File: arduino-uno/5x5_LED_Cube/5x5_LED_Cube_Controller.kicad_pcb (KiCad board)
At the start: 2 copper layers, 11 parts, among them Q1 DMG2305UX, Q2 DMG2305UX, Q3 DMG2305UX, Q4 DMG2305UX, Q5 DMG2305UX, U1 TLC5940NT, U2 TLC5940NT

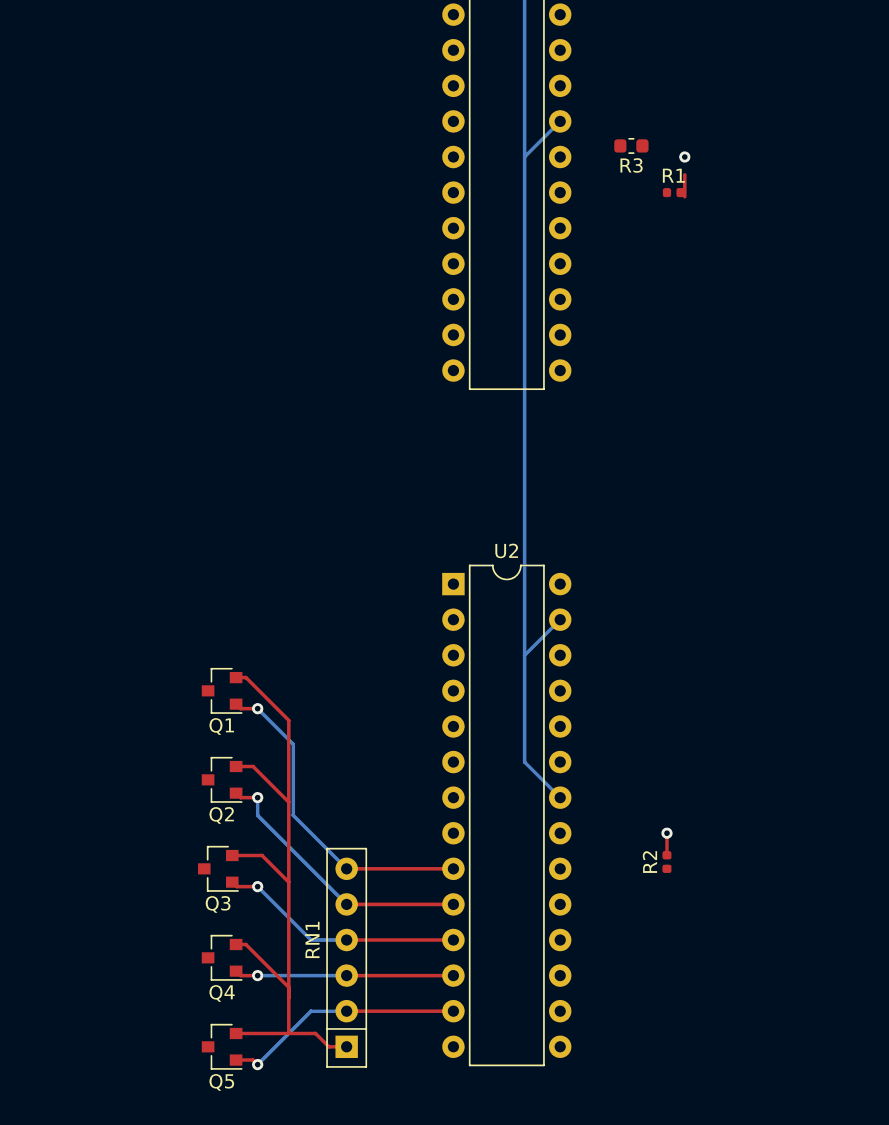
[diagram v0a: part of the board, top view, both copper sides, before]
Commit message: Added headers for layers and arduino input
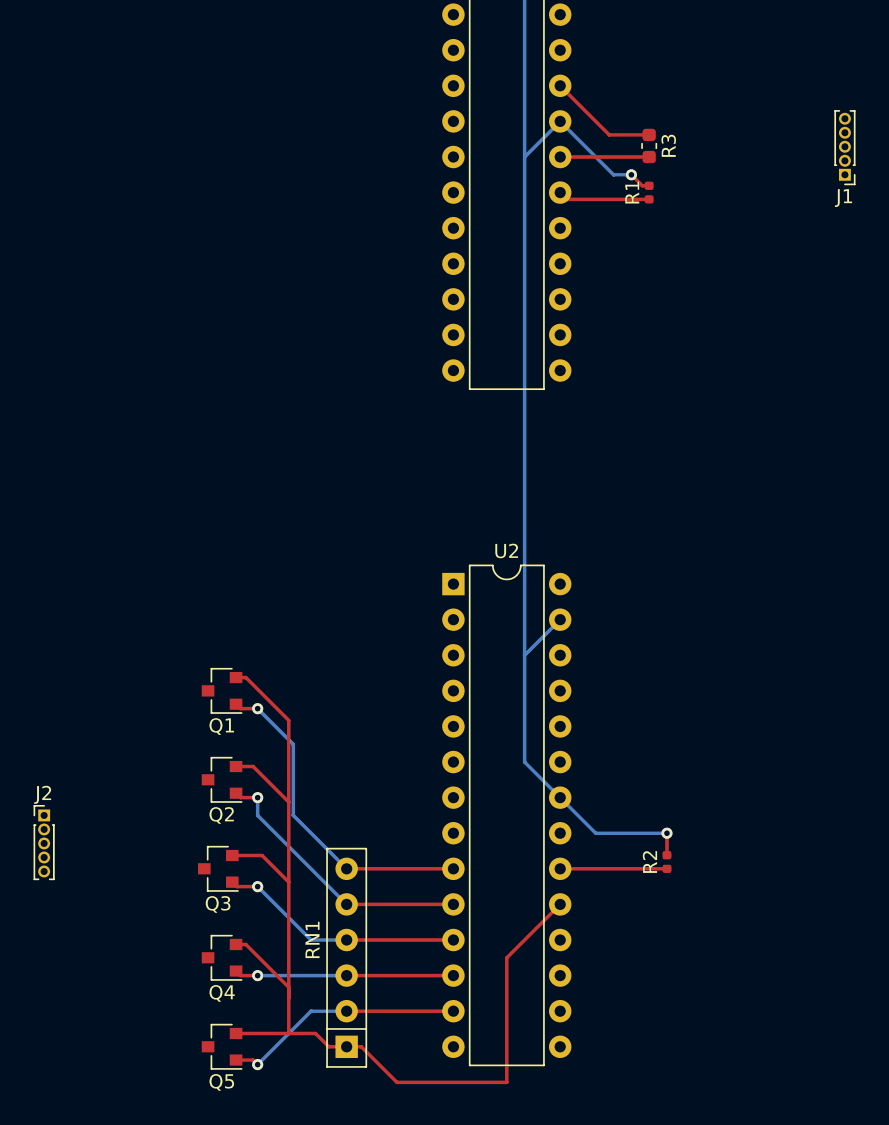
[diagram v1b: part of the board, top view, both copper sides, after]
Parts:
- added J1: Conn_01x05, Connector_PinHeader_1.00mm:PinHeader_1x05_P1.00mm_Vertical, F.Cu at (246.4, 61.0)
- added J2: Conn_01x05, Connector_PinHeader_1.00mm:PinHeader_1x05_P1.00mm_Vertical, F.Cu at (189.2, 106.7)
- moved R1 1.75 mm to (232.4, 62.2), turned to 90 degrees
- moved R3 1.27 mm to (232.4, 58.9), turned to 270 degrees
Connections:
- Q1 pad 3: /5x5_LED_Cube_Matrix/Layer1 -> /Layer1
- Q2 pad 3: /5x5_LED_Cube_Matrix/Layer2 -> /Layer2
- Q3 pad 3: /5x5_LED_Cube_Matrix/Layer3 -> /Layer3
- Q4 pad 3: /5x5_LED_Cube_Matrix/Layer4 -> /Layer4
- Q5 pad 3: /5x5_LED_Cube_Matrix/Layer5 -> /Layer5
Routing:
- net +5V: track 51.1 -> 84.2 mm
- net GND: track 73.4 -> 88.7 mm
- net /ArduinoD10: track 0.00 -> 7.80 mm
- net Net-(R2-Pad1): track 0.00 -> 7.62 mm
- net Net-(R1-Pad1): track 0.00 -> 6.55 mm

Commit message: Updated PCB to latest schematic changes
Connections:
- net /5x5_LED_Cube_Matrix/LED1 renamed /LED1
- net /5x5_LED_Cube_Matrix/LED10 renamed /LED10
- net /5x5_LED_Cube_Matrix/LED11 renamed /LED11
- net /5x5_LED_Cube_Matrix/LED12 renamed /LED12
- net /5x5_LED_Cube_Matrix/LED13 renamed /LED13
- net /5x5_LED_Cube_Matrix/LED14 renamed /LED14
- net /5x5_LED_Cube_Matrix/LED15 renamed /LED15
- net /5x5_LED_Cube_Matrix/LED16 renamed /LED16
- net /5x5_LED_Cube_Matrix/LED17 renamed /LED17
- net /5x5_LED_Cube_Matrix/LED18 renamed /LED18
- net /5x5_LED_Cube_Matrix/LED19 renamed /LED19
- net /5x5_LED_Cube_Matrix/LED2 renamed /LED2
- net /5x5_LED_Cube_Matrix/LED20 renamed /LED20
- net /5x5_LED_Cube_Matrix/LED21 renamed /LED21
- net /5x5_LED_Cube_Matrix/LED22 renamed /LED22
- net /5x5_LED_Cube_Matrix/LED23 renamed /LED23
- net /5x5_LED_Cube_Matrix/LED24 renamed /LED24
- net /5x5_LED_Cube_Matrix/LED25 renamed /LED25
- net /5x5_LED_Cube_Matrix/LED3 renamed /LED3
- net /5x5_LED_Cube_Matrix/LED4 renamed /LED4
- net /5x5_LED_Cube_Matrix/LED5 renamed /LED5
- net /5x5_LED_Cube_Matrix/LED6 renamed /LED6
- net /5x5_LED_Cube_Matrix/LED7 renamed /LED7
- net /5x5_LED_Cube_Matrix/LED8 renamed /LED8
- net /5x5_LED_Cube_Matrix/LED9 renamed /LED9
- net Net-(Q1-Pad1) renamed /Layer1Gate
- net Net-(Q2-Pad1) renamed /Layer2Gate
- net Net-(Q3-Pad1) renamed /Layer3Gate
- net Net-(Q4-Pad1) renamed /Layer4Gate
- net Net-(Q5-Pad1) renamed /Layer5Gate
- net Net-(R1-Pad1) renamed /IREF1
- net Net-(R2-Pad1) renamed /IREF2

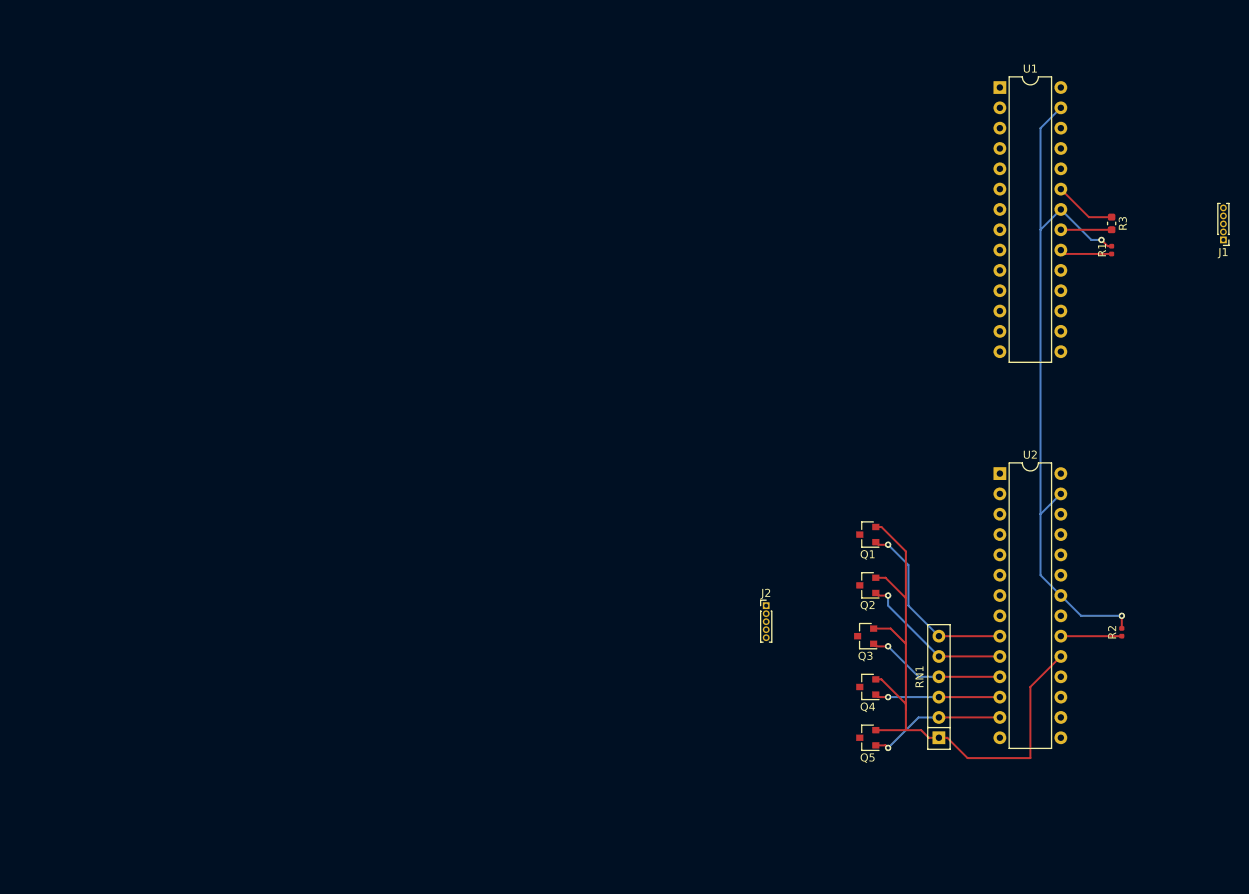
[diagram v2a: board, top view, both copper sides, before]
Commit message: Routed more PCB traces and added power header
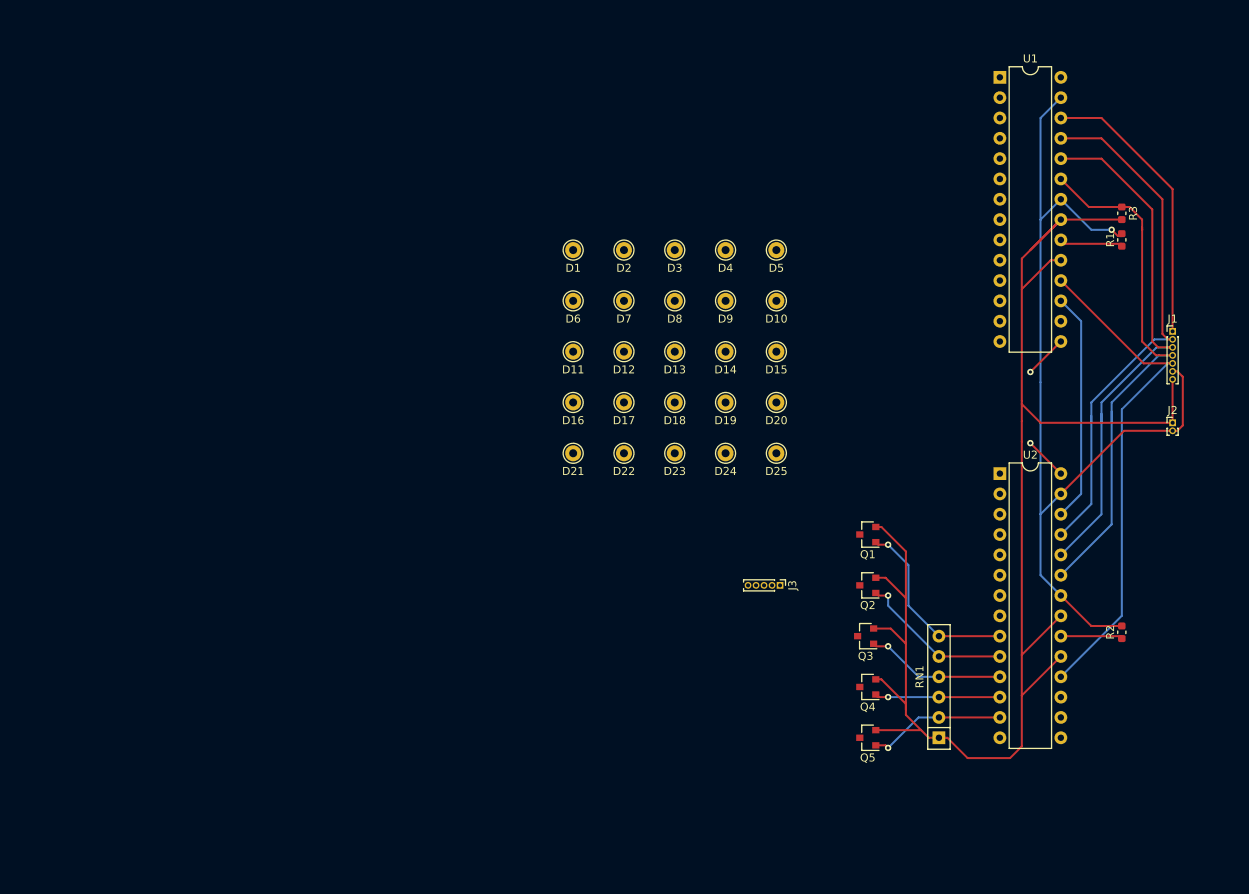
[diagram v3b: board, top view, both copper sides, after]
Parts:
- added D1: LED, Connector_Pin:Pin_D1.0mm_L10.0mm, F.Cu at (165.1, 62.2)
- added D10: LED, Connector_Pin:Pin_D1.0mm_L10.0mm, F.Cu at (190.5, 68.6)
- added D11: LED, Connector_Pin:Pin_D1.0mm_L10.0mm, F.Cu at (165.1, 74.9)
- added D12: LED, Connector_Pin:Pin_D1.0mm_L10.0mm, F.Cu at (171.4, 74.9)
- added D13: LED, Connector_Pin:Pin_D1.0mm_L10.0mm, F.Cu at (177.8, 74.9)
- added D14: LED, Connector_Pin:Pin_D1.0mm_L10.0mm, F.Cu at (184.2, 74.9)
- added D15: LED, Connector_Pin:Pin_D1.0mm_L10.0mm, F.Cu at (190.5, 74.9)
- added D16: LED, Connector_Pin:Pin_D1.0mm_L10.0mm, F.Cu at (165.1, 81.3)
- added D17: LED, Connector_Pin:Pin_D1.0mm_L10.0mm, F.Cu at (171.4, 81.3)
- added D18: LED, Connector_Pin:Pin_D1.0mm_L10.0mm, F.Cu at (177.8, 81.3)
- added D19: LED, Connector_Pin:Pin_D1.0mm_L10.0mm, F.Cu at (184.2, 81.3)
- added D2: LED, Connector_Pin:Pin_D1.0mm_L10.0mm, F.Cu at (171.4, 62.2)
- added D20: LED, Connector_Pin:Pin_D1.0mm_L10.0mm, F.Cu at (190.5, 81.3)
- added D21: LED, Connector_Pin:Pin_D1.0mm_L10.0mm, F.Cu at (165.1, 87.6)
- added D22: LED, Connector_Pin:Pin_D1.0mm_L10.0mm, F.Cu at (171.4, 87.6)
- added D23: LED, Connector_Pin:Pin_D1.0mm_L10.0mm, F.Cu at (177.8, 87.6)
- added D24: LED, Connector_Pin:Pin_D1.0mm_L10.0mm, F.Cu at (184.2, 87.6)
- added D25: LED, Connector_Pin:Pin_D1.0mm_L10.0mm, F.Cu at (190.5, 87.6)
- added D3: LED, Connector_Pin:Pin_D1.0mm_L10.0mm, F.Cu at (177.8, 62.2)
- added D4: LED, Connector_Pin:Pin_D1.0mm_L10.0mm, F.Cu at (184.2, 62.2)
- added D5: LED, Connector_Pin:Pin_D1.0mm_L10.0mm, F.Cu at (190.5, 62.2)
- added D6: LED, Connector_Pin:Pin_D1.0mm_L10.0mm, F.Cu at (165.1, 68.6)
- added D7: LED, Connector_Pin:Pin_D1.0mm_L10.0mm, F.Cu at (171.4, 68.6)
- added D8: LED, Connector_Pin:Pin_D1.0mm_L10.0mm, F.Cu at (177.8, 68.6)
- added D9: LED, Connector_Pin:Pin_D1.0mm_L10.0mm, F.Cu at (184.2, 68.6)
- added J2: Power, Connector_PinHeader_1.00mm:PinHeader_1x02_P1.00mm_Vertical, F.Cu at (240.0, 83.8)
- J1: value Conn_01x05 -> Arduino; footprint Connector_PinHeader_1.00mm:PinHeader_1x05_P1.00mm_Vertical -> Connector_PinHeader_1.00mm:PinHeader_1x07_P1.00mm_Vertical
- J3: renamed from J2; value Conn_01x05 -> Layers
- R1, R2: footprint Resistor_SMD:R_0402_1005Metric -> Resistor_SMD:R_0603_1608Metric
- moved J1 13.1 mm to (240.0, 72.4), turned to 0 degrees
- moved J3 3.07 mm to (191.0, 104.1), turned to 270 degrees
- moved R3 1.80 mm to (233.7, 57.6)
- moved R1 1.80 mm to (233.7, 61.0)
- moved U1 1.27 mm to (218.4, 40.6)
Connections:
- J1 pad 1: /ArduinoD3 -> /ArduinoD11(SIN)
- J1 pad 2: /ArduinoD9 -> /ArduinoD13(SCLK)
- J1 pad 3: /ArduinoD10 -> /ArduinoD9(XLAT)
- J1 pad 4: /ArduinoD11 -> /ArduinoD10(BLANK)
- J1 pad 5: /ArduinoD13 -> /ArduinoD3(GSCLK)
- R3 pad 1: /ArduinoD10 -> /ArduinoD10(BLANK)
- U1 pad 17: Net-(U1-Pad17) -> /SOUT1
- U1 pad 18: /ArduinoD3 -> /ArduinoD3(GSCLK)
- U1 pad 23: /ArduinoD10 -> /ArduinoD10(BLANK)
- U1 pad 24: /ArduinoD9 -> /ArduinoD9(XLAT)
- U1 pad 25: /ArduinoD13 -> /ArduinoD13(SCLK)
- U1 pad 26: Net-(U1-Pad26) -> /ArduinoD11(SIN)
- U2 pad 17: Net-(U1-Pad26) -> Net-(U2-Pad17)
- U2 pad 18: /ArduinoD3 -> /ArduinoD3(GSCLK)
- U2 pad 23: /ArduinoD10 -> /ArduinoD10(BLANK)
- U2 pad 24: /ArduinoD9 -> /ArduinoD9(XLAT)
- U2 pad 25: /ArduinoD13 -> /ArduinoD13(SCLK)
- U2 pad 26: /ArduinoD11 -> /SOUT1
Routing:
- net +5V: track 84.2 -> 192.0 mm
- net /ArduinoD9(XLAT): track 0.00 -> 68.1 mm
- net /ArduinoD10(BLANK): track 0.00 -> 68.0 mm
- net /ArduinoD13(SCLK): track 0.00 -> 66.6 mm
- net /ArduinoD3(GSCLK): track 0.00 -> 63.6 mm
- net /ArduinoD11(SIN): track 0.00 -> 35.4 mm
- net /SOUT1: track 0.00 -> 28.8 mm
- net GND: track 88.7 -> 116.7 mm, vias 2 -> 1
- net /ArduinoD10: track 7.80 -> 0.00 mm
- net /LED17: track 0.00 -> 5.39 mm, vias 0 -> 1
- net /LED16: track 0.00 -> 5.39 mm, vias 0 -> 1
- net /IREF1: track 6.55 -> 7.82 mm

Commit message: Finished PCB routing
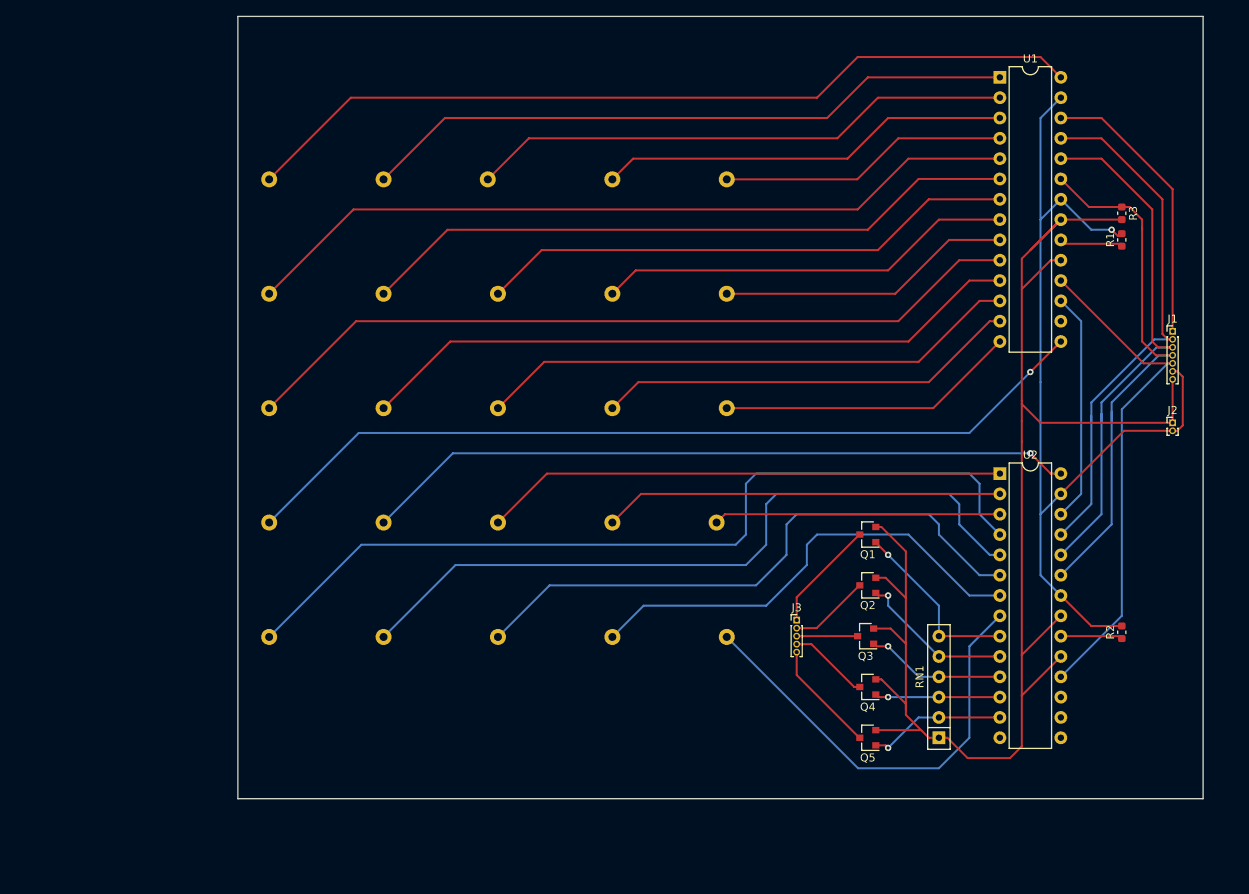
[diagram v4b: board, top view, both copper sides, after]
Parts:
- D1, D10, D11, D12, D13, D14, D15, D16, D17, D18, D19, D2, D20, D21, D22, D23, D24, D25, D3, D4, D5, D6, D7, D8, D9: moved to B.Cu
- moved D21 44.4 mm to (127.1, 110.6)
- moved D16 40.9 mm to (127.1, 96.3)
- moved D1 39.0 mm to (127.1, 53.4)
- moved D11 38.7 mm to (127.1, 82.0)
- moved D6 38.0 mm to (127.1, 67.7)
- moved D22 37.8 mm to (141.4, 110.6)
- moved D17 33.6 mm to (141.4, 96.3)
- moved D23 31.9 mm to (155.7, 110.6)
- moved D2 31.3 mm to (141.4, 53.4)
- moved D12 30.9 mm to (141.4, 82.0)
- moved D7 30.1 mm to (141.4, 67.7)
- moved D24 27.0 mm to (170.0, 110.6)
- moved D18 26.7 mm to (155.7, 96.3)
- moved D3 25.0 mm to (154.4, 53.4)
- moved D25 23.8 mm to (184.3, 110.6)
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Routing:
- net /LED21: track 0.00 -> 108.9 mm
- net /LED1: track 0.00 -> 106.3 mm
- net /LED16: track 5.39 -> 108.3 mm
- net /LED11: track 0.00 -> 99.0 mm
- net /LED6: track 0.00 -> 98.3 mm
- net /LED22: track 0.00 -> 92.1 mm
- net /LED17: track 5.39 -> 89.3 mm
- net /LED12: track 0.00 -> 83.6 mm
- net /LED7: track 0.00 -> 83.0 mm
- net /LED2: track 0.00 -> 82.3 mm
- net /LED23: track 0.00 -> 75.2 mm
- net /LED13: track 0.00 -> 68.3 mm
- net /LED3: track 0.00 -> 68.2 mm
- net /LED8: track 0.00 -> 67.6 mm
- net /LED18: track 0.00 -> 65.3 mm
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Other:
- board outline added: 120.7 x 97.8 mm

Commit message: Removed traces and rearannged footprints a little
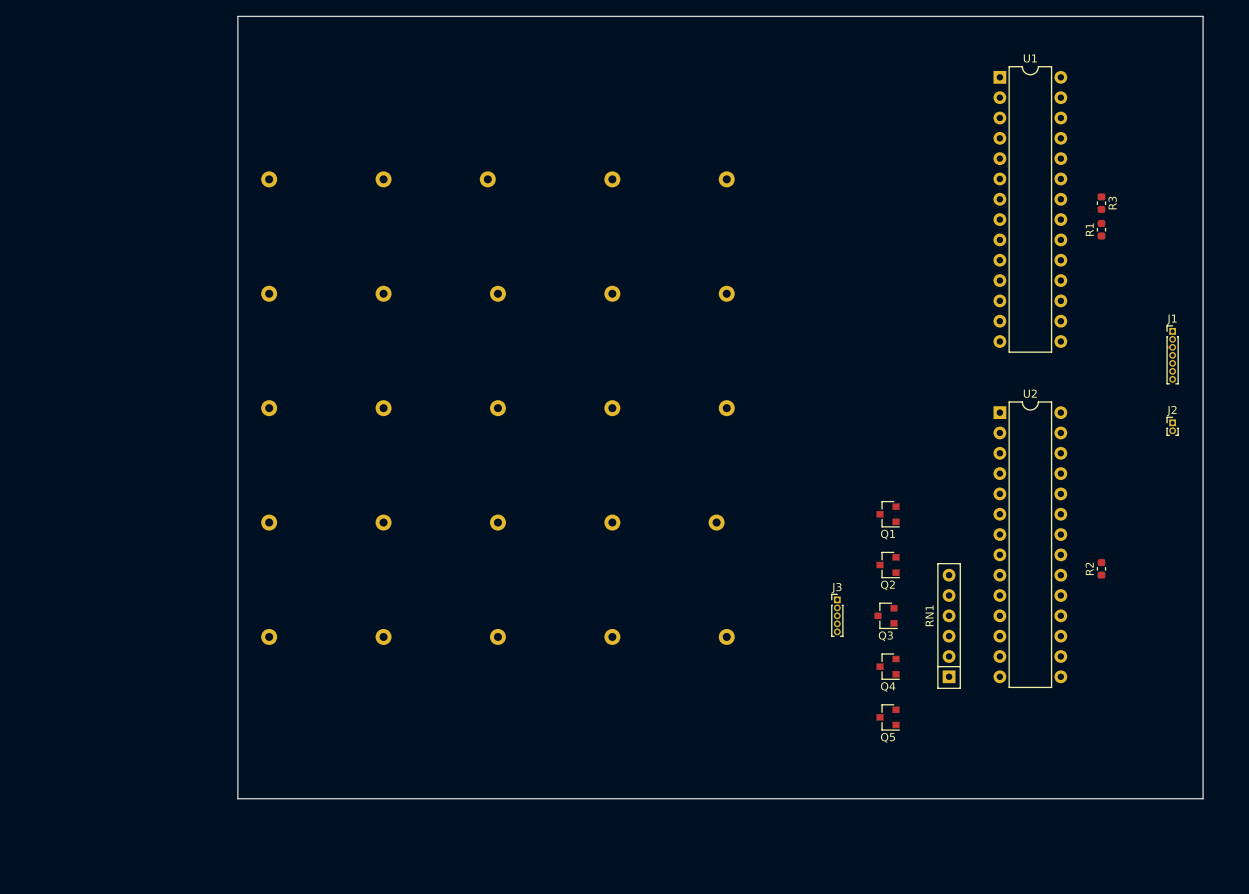
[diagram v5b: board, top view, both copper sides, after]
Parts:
- moved R2 8.32 mm to (231.1, 102.1)
- moved RN1 7.73 mm to (212.1, 115.6)
- moved U2 7.62 mm to (218.4, 82.5)
- moved J3 5.68 mm to (198.1, 106.0)
- moved Q1 3.59 mm to (204.5, 95.2)
- moved Q2 3.59 mm to (204.5, 101.6)
- moved Q4 3.59 mm to (204.5, 114.3)
- moved Q3 3.59 mm to (204.2, 108.0)
- moved Q5 3.59 mm to (204.5, 120.7)
- moved R1 2.84 mm to (231.1, 59.7)
- moved R3 2.84 mm to (231.1, 56.4)
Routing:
- net +5V: track 192.0 -> 0.00 mm
- net GND: track 116.7 -> 0.00 mm, vias 1 -> 0
- net /LED21: track 108.9 -> 0.00 mm
- net /LED16: track 108.3 -> 0.00 mm, vias 1 -> 0
- net /LED1: track 106.3 -> 0.00 mm
- net /LED11: track 99.0 -> 0.00 mm
- net /LED6: track 98.3 -> 0.00 mm
- net /LED22: track 92.1 -> 0.00 mm
- net /LED17: track 89.3 -> 0.00 mm, vias 1 -> 0
- net /LED12: track 83.6 -> 0.00 mm
- net /LED7: track 83.0 -> 0.00 mm
- net /LED2: track 82.3 -> 0.00 mm
- net /LED23: track 75.2 -> 0.00 mm
- net /LED13: track 68.3 -> 0.00 mm
- net /LED3: track 68.2 -> 0.00 mm
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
